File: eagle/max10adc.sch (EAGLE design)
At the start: 173 parts, among them IC1 MAX19506, IC2 MAX19506, J1 MOLEX_BNC_73100-0105, J2 MOLEX_BNC_73100-0105, J3 MOLEX_BNC_73100-0105, J4 MOLEX_BNC_73100-0105, K1 AQY21SOP, K2 AQY21SOP, K3 AQY21SOP, K4 AQY21SOP, K5 AQY21SOP, K6 AQY21SOP, K7 AQY21SOP, K8 AQY21SOP, U1 MAX4416ESA, U2 MAX4416ESA, U340G CH340G, Y1 ABL-12.000MHZ-B2

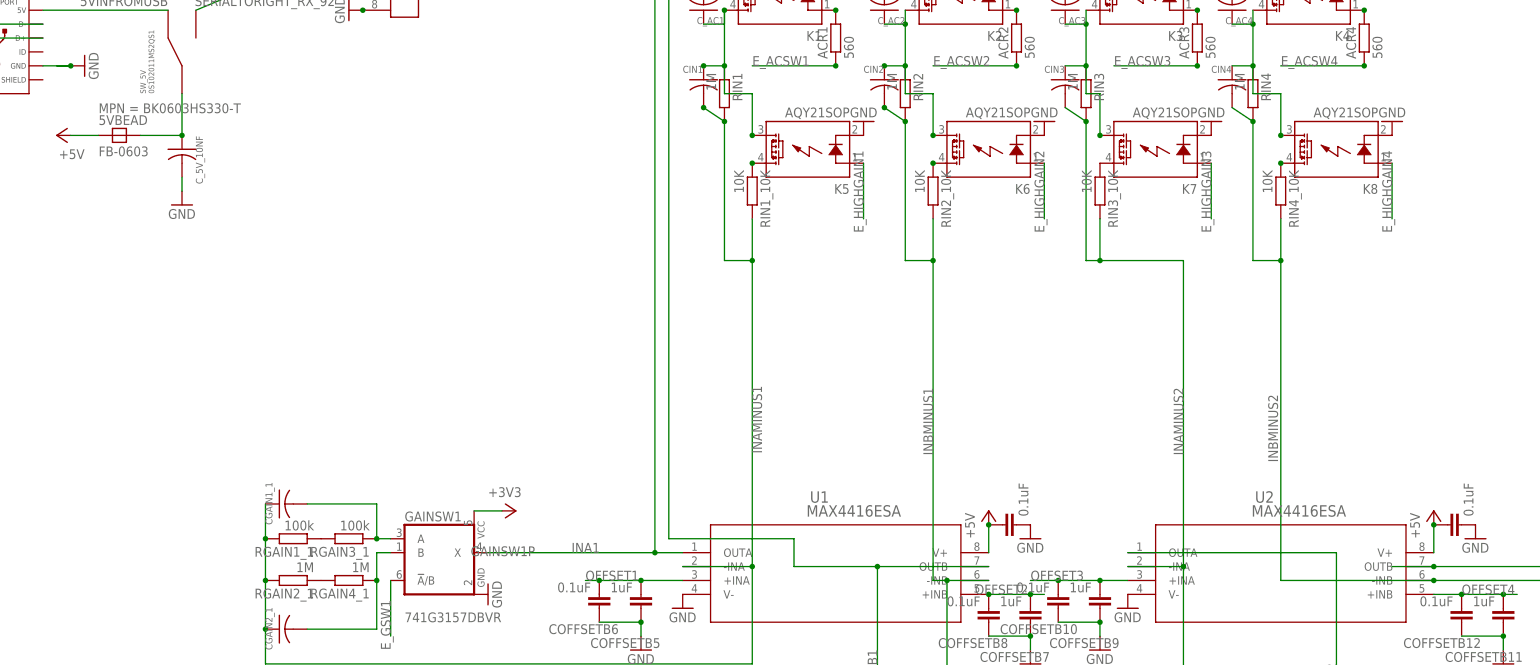
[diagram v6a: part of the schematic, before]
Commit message: updates for v8.5 and v8.6
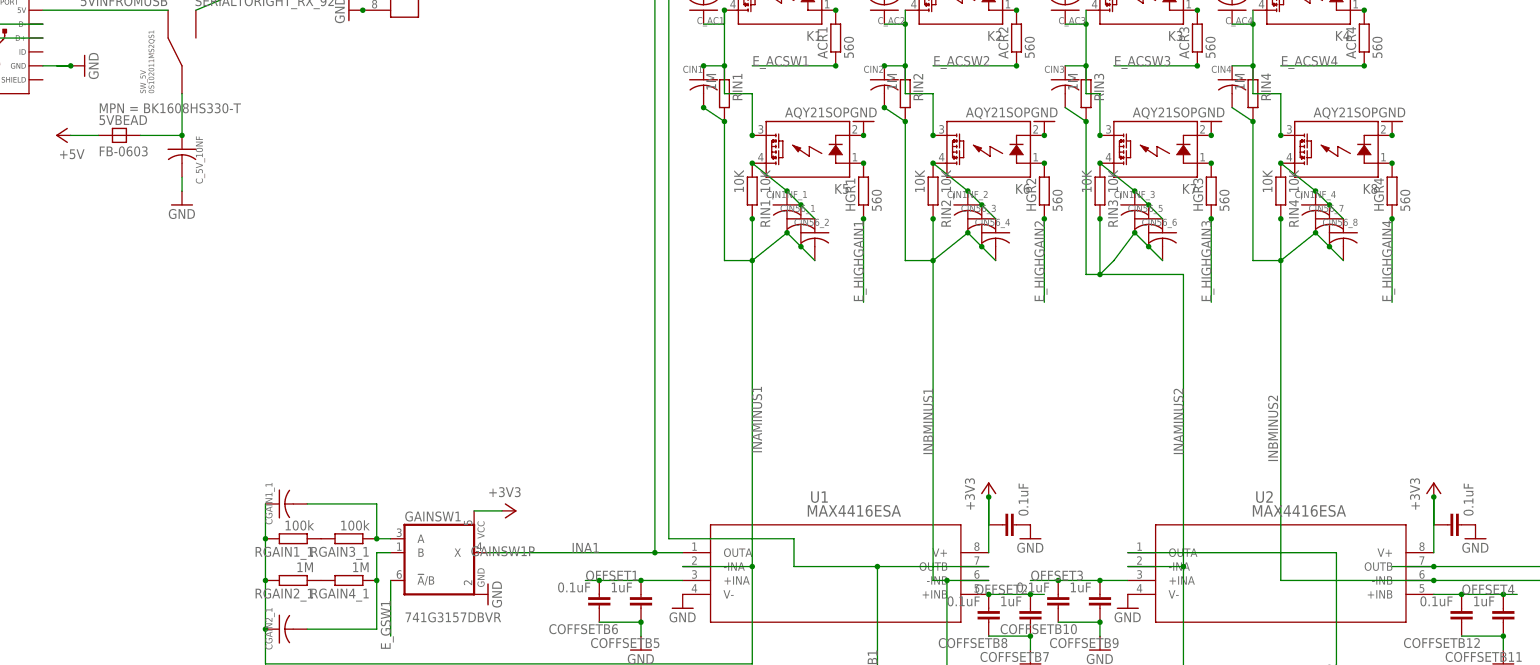
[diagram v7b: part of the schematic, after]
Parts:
- added CIN1NF_1, CIN1NF_2, CIN1NF_3, CIN1NF_4: 1nF, rcl@1:C-USC0603
- added CIN56_1, CIN56_2, CIN56_3, CIN56_4, CIN56_5, CIN56_6, CIN56_7, CIN56_8: 56pF, rcl@1:C-USC0603
- added HGR1, HGR2, HGR3, HGR4: 560, resistor:R-EU_R0805
- 5VBEAD: MPN BK0603HS330-T -> BK1608HS330-T
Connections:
- new net N$34: HGR1.2, K5.A
- new net N$36: HGR2.2, K6.A
- new net N$37: HGR3.2, K7.A
- new net N$43: HGR4.2, K8.A
- net +3V3: now also C5VOPAMP1.1, C5VOPAMP2.1, U1.V+, U2.V+
- net +5V: no longer C5VOPAMP1.1, C5VOPAMP2.1, U1.V+, U2.V+
- net E_HIGHGAIN1: now also HGR1.1; no longer K5.A
- net E_HIGHGAIN2: now also HGR2.1; no longer K6.A
- net E_HIGHGAIN3: now also HGR3.1; no longer K7.A
- net E_HIGHGAIN4: now also HGR4.1; no longer K8.A
- net INAMINUS1: now also CIN1NF_1.2, CIN56_1.2, CIN56_2.2
- net INAMINUS2: now also CIN1NF_3.2, CIN56_5.2, CIN56_6.2
- net INBMINUS1: now also CIN1NF_2.2, CIN56_3.2, CIN56_4.2
- net INBMINUS2: now also CIN1NF_4.2, CIN56_7.2, CIN56_8.2
- net N$20: now also CIN1NF_1.1, CIN56_1.1, CIN56_2.1
- net N$38: now also CIN1NF_2.1, CIN56_3.1, CIN56_4.1
- net N$40: now also CIN1NF_3.1, CIN56_5.1, CIN56_6.1
- net N$42: now also CIN1NF_4.1, CIN56_7.1, CIN56_8.1

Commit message: for 8.7 with separate VCCA
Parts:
- removed 5VBEAD: FB-0603, rcl:FB-0603
- added CP10, CP11, CP7, CP9: 1uF, rcl:C-EUC0805K
- added CP3, CP4: 10uF, rcl@1:C-USC1206
- added CP8: 0.1uF, rcl:C-EUC0805K
- added C_5V_10NF1: 0.01uF, rcl@1:C-USC0603
- added L1, L2: 10uH, SparkFun-Passives:INDUCTOR1210
- added REG1: LDL1117S33R, Seeed-IC-2016:PMIC-CJT1117-3.3(SOT223)
- added ROFFSET1, ROFFSET2, ROFFSET3, ROFFSET4: 200, rcl@1:R-US_R0805
- COFFSETB11, COFFSETB5, COFFSETB7, COFFSETB9: value 1uF -> 10uF; MPN MF-CAP-0805-1uF -> MF-CAP-0805-10uF
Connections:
- removed net 5V_IN: 5VBEAD.2, C_5V_10NF.1, SW_5V.C
- new net N$44: DAC1.VOUT_A, ROFFSET1.2
- new net N$45: DAC1.VOUT_B, ROFFSET2.2
- new net N$46: DAC1.VOUT_C, ROFFSET3.2
- new net N$47: DAC1.VOUT_D, ROFFSET4.2
- new net N$48: CP3.1, CP7.1, CP8.1, L2.2, REG1.IN
- new net N$49: CP1.1, CP2.1, CP5.1, L1.2, REG.IN
- new net VCCA: C5VOPAMP1.1, C5VOPAMP2.1, CADD1_A.1, CADD1_B.1, CADD2_A.1, CADD2_B.1, COFFSET.2, CP4.1, CP9.1, DAC1.VDD, GAINSW1P.VCC, GAINSW2P.VCC, GAINSW3P.VCC, GAINSW4P.VCC, IC1.AVDD1, IC1.AVDD2, IC2.AVDD1, IC2.AVDD2, OVSAMP1P.VCC, OVSAMP2P.VCC, REG1.OUT, U1.V+, U2.V+
- net +3V3: no longer C5VOPAMP1.1, C5VOPAMP2.1, CADD1_A.1, CADD1_B.1, CADD2_A.1, CADD2_B.1, COFFSET.2, DAC1.VDD, GAINSW1P.VCC, GAINSW2P.VCC, GAINSW3P.VCC, GAINSW4P.VCC, IC1.AVDD1, IC1.AVDD2, IC2.AVDD1, IC2.AVDD2, OVSAMP1P.VCC, OVSAMP2P.VCC, U1.V+, U2.V+
- net +5V: now also CP10.2, CP11.2, C_5V_10NF.2, C_5V_10NF1.2, L1.1, L2.1, SW_5V.C; no longer 5VBEAD.1, CP1.1, CP2.1, CP5.1, REG.IN
- net GND: now also CP10.1, CP11.1, CP3.2, CP4.2, CP7.2, CP8.2, CP9.2, C_5V_10NF.1, C_5V_10NF1.1, REG1.GND; no longer C_5V_10NF.2
- net OFFSET1: now also ROFFSET1.1; no longer DAC1.VOUT_A
- net OFFSET2: now also ROFFSET2.1; no longer DAC1.VOUT_B
- net OFFSET3: now also ROFFSET3.1; no longer DAC1.VOUT_C
- net OFFSET4: now also ROFFSET4.1; no longer DAC1.VOUT_D
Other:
- moved on the sheet: C_5V_10NF
